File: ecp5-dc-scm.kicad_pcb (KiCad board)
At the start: 8 copper layers, 90 x 120.4 mm, 463 parts, among them IC1 TPS54561, J1 L834-1G1T-S7, J2 1-2199230-6, J3 543630489, J4 M20-7830642, J5 SFF-TA-1002-4C+, J6 0878311420, J7 61300611121, J8 S2B-PH-K-S_LF__SN_, Q1 2N7002, Q10 2N7002, Q11 2N7002, Q12 2N7002, Q13 2N7002, Q14 2N7002, Q15 2N7002, Q16 2N7002, Q17 2N7002, Q2 2N7002, Q3 2N7002, Q4 IRLML6402TRPBF, Q5 IRLML6402TRPBF, Q6 IRLML6402TRPBF, Q7 IRLML6402TRPBF, Q8 IRLML6402TRPBF, Q9 IRLML6402TRPBF, U1 KSZ9031RNXCA, U10 AS4C256M16D3, U11 TPS51200DRC, U12 LM3881MME_NOPB, U13 LM21212-2, U14 SN74LVC1G11DBVR, U16 TPS62823DLCT, U17 TPS62823DLCT, U18 TPS62823DLCT, U19 TPS62823DLCT, U2 W25Q32JVSSIQ_TR, U20 TPS62823DLCT, U21 ECP5UM5G_85_CABGA756, U3 W25Q32JVSSIQ_TR, U4 W25Q32JVSSIQ_TR, U5 W25Q32JVSSIQ_TR, U6 MTFC32GAPALBH-AIT, U7 NVT2008DQ,115, U8 USB3300-EZK-TR, U9 USB3300-EZK-TR, Y1 ABM8G-25.000MHZ-18-D2Y-T, Y2 TSX-3225, Y3 TSX-3225

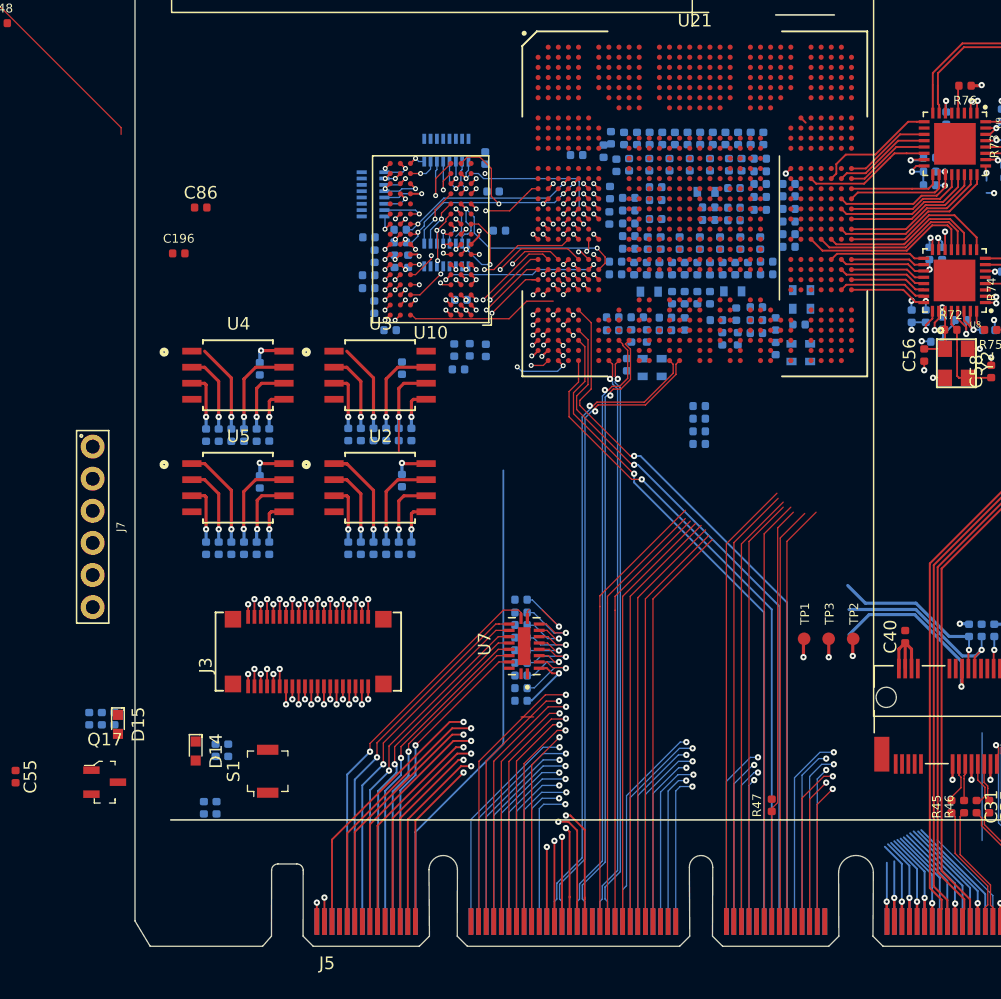
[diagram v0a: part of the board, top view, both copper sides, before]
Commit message: Routed NCSI chip corner
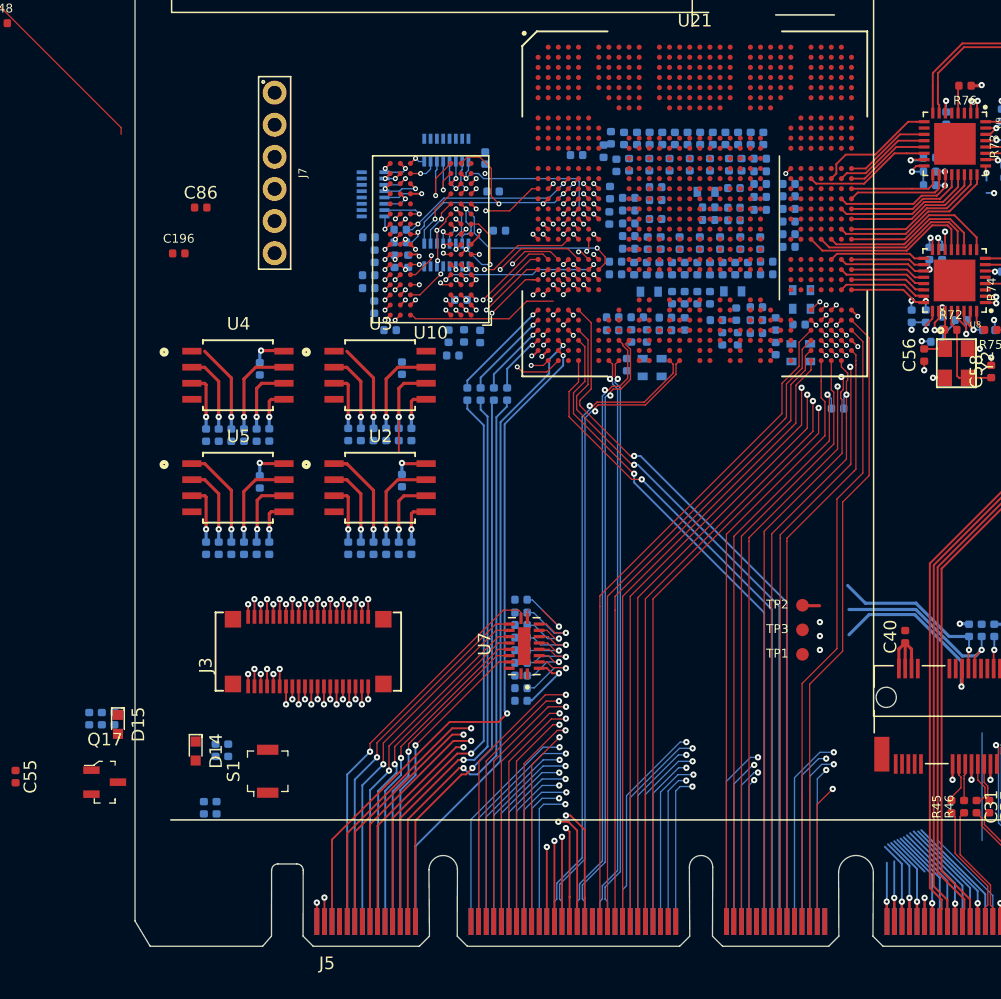
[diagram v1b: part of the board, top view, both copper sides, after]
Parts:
- R47: moved to B.Cu
- moved R47 31.8 mm to (115.7, 136.8), turned to 180 degrees
- moved J7 31.5 mm to (71.2, 118.1)
- moved R132 18.4 mm to (86.4, 135.6), turned to 90 degrees
- moved R133 17.7 mm to (87.5, 135.6), turned to 90 degrees
- moved R135 16.5 mm to (88.5, 135.6), turned to 90 degrees
- moved R134 15.3 mm to (89.5, 135.6), turned to 90 degrees
- moved TP2 4.88 mm to (112.9, 152.3), turned to 180 degrees
- moved TP3 2.26 mm to (112.9, 154.2), turned to 180 degrees
- moved TP1 1.19 mm to (112.9, 156.1), turned to 180 degrees
- moved C80 1.19 mm to (87.4, 131.0)
- moved C84 1.19 mm to (85.2, 132.6)
- moved C85 1.19 mm to (86.1, 131.0)
- moved C87 1.19 mm to (84.9, 131.0)
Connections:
- U21 pad AG28: QSPI1_CS0_N -> QSPI1_D0
- U21 pad AG29: SGPIO0_CLK -> QSPI1_D1
- U21 pad AG30: SGPIO1_CLK -> QSPI1_D2
- U21 pad AG32: SGPIO_RESET_N -> QSPI1_D3
- U21 pad AH28: SGPIO0_DI -> NCSI_TXD1
- U21 pad AH30: SGPIO0_DO -> NCSI_RXER
- U21 pad AH32: SGPIO1_DO -> SGPIO_INTR_N
- U21 pad AJ28: QSPI1_CLK -> NCSI_CLK
- U21 pad AJ29: SGPIO1_LD -> NCSI_RXD0
- U21 pad AJ30: SGPIO_INTR_N -> SGPIO1_DO
- U21 pad AJ31: QSPI1_D1 -> QSPI1_CLK
- U21 pad AJ32: NCSI_TXD0 -> SGPIO_RESET_N
- U21 pad AK29: SGPIO0_LD -> NCSI_RXD1
- U21 pad AK30: SGPIO1_DI -> SGPIO0_CLK
- U21 pad AK31: QSPI1_D3 -> SGPIO1_DI
- U21 pad AK32: NCSI_TXEN -> QSPI1_CS0_N
- U21 pad AL28: NCSI_RXD1 -> NCSI_TXEN
- U21 pad AL30: NCSI_TXD1 -> SGPIO0_LD
- U21 pad AL32: QSPI1_D0 -> SGPIO1_LD
- U21 pad AM28: NCSI_RXD0 -> NCSI_TXD0
- U21 pad AM29: NCSI_CLK -> SGPIO0_DO
- U21 pad AM30: NCSI_RXER -> SGPIO0_DI
- U21 pad AM31: QSPI1_D2 -> SGPIO1_CLK
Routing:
- net (no net): track 49.1 -> 145.2 mm
- net SGPIO_INTR_N: track 42.2 -> 100.6 mm, vias 1 -> 0
- net SGPIO_RESET_N: track 42.2 -> 97.3 mm, vias 1 -> 0
- net I2C[11]_SCL: track 42.7 -> 93.7 mm
- net I2C[12]_SCL: track 42.1 -> 92.5 mm
- net I2C[12]_SDA: track 41.6 -> 92.0 mm
- net I2C[11]_SDA: track 42.7 -> 93.0 mm
- net I2C[9]_SDA: track 46.6 -> 96.1 mm
- net I2C[10]_SDA: track 45.8 -> 95.2 mm
- net I2C[10]_SCL: track 46.3 -> 95.5 mm
- net UART1_SCM_RX: track 64.9 -> 113.0 mm
- net I3C[3]_SDA_3V3: track 41.5 -> 89.5 mm
- net UART0_SCM_TX: track 64.2 -> 112.2 mm
- net ESPI_CS1_N: track 61.3 -> 109.3 mm
- net I3C[2]_SDA_3V3: track 40.2 -> 88.3 mm
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
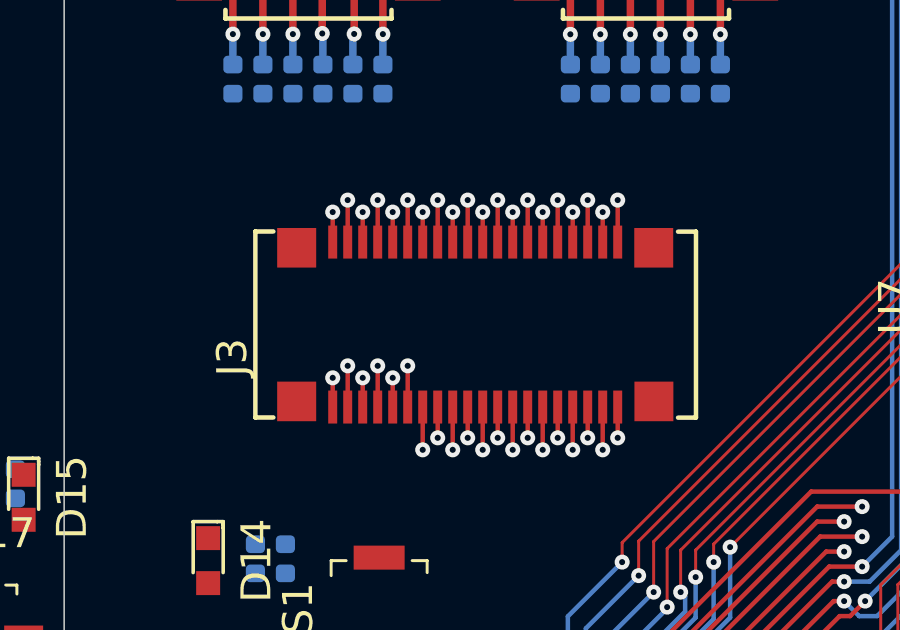
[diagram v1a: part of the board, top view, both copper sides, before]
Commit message: Updated RoT connector
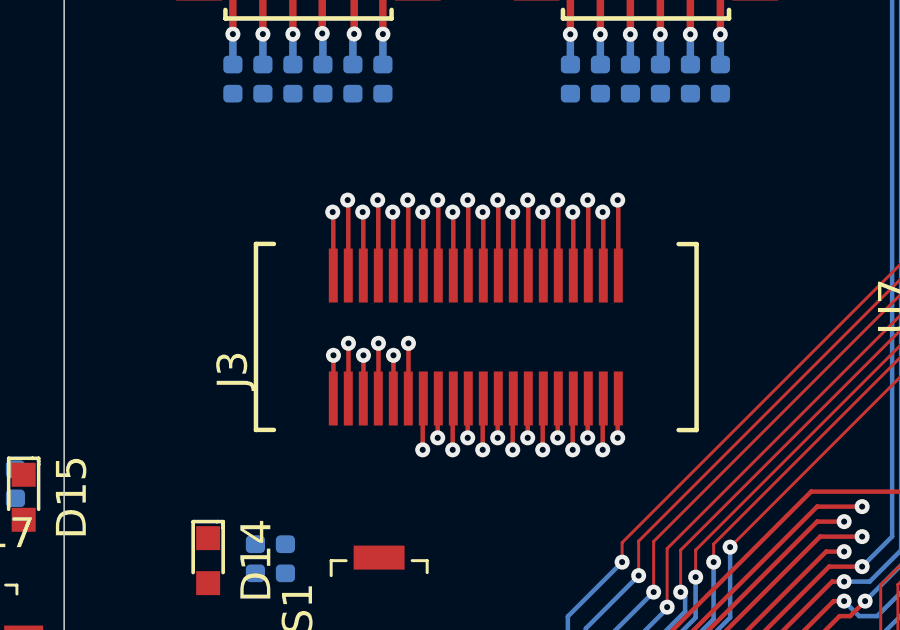
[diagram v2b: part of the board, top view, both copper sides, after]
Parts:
- J3: value 543630489 -> 529910408; footprint ecp5-dc-scm-footprints:543630489 -> ecp5-dc-scm-footprints:529910408
- moved J3 0.42 mm to (73.8, 156.4)
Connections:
- U21 pad A14: RGMII_TXD0 -> Net-(U21-PadA14)
- U21 pad A16: RGMII_RXD0 -> Net-(U21-PadA16)
- U21 pad A17: RGMII_RX_CLK -> Net-(U21-PadA17)
- U21 pad A8: RGMII_TXD1 -> Net-(U21-PadA8)
- U21 pad B16: ETH_MDC -> Net-(U21-PadB16)
- U21 pad B17: RGMII_REF_CLK -> Net-(U21-PadB17)
- U21 pad B8: RGMII_TXD2 -> Net-(U21-PadB8)
- U21 pad C16: RGMII_RX_DV -> Net-(U21-PadC16)
- U21 pad C17: RGMII_TX_CLK -> Net-(U21-PadC17)
- U21 pad C8: RGMII_RXD3 -> Net-(U21-PadC8)
- U21 pad D15: RGMII_TX_EN -> Net-(U21-PadD15)
- U21 pad D16: RGMII_RXD1 -> Net-(U21-PadD16)
- U21 pad D8: RGMII_TXD3 -> Net-(U21-PadD8)
- U21 pad E16: RGMII_RXD2 -> Net-(U21-PadE16)
- U21 pad K12: VCC3V3_T -> Net-(U21-PadK12)
- U21 pad K14: VCC3V3_T -> Net-(U21-PadK14)
- U21 pad K15: VCC3V3_T -> Net-(U21-PadK15)
- U21 pad K16: VCC3V3_T -> Net-(U21-PadK16)
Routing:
- net QSPI0_CS1_N: track 1.40 -> 2.52 mm
- net QSPIA2_D2: track 23.4 -> 24.5 mm
- net VCC3V3: track 64.6 -> 65.7 mm
- net QSPIA2_D1: track 24.7 -> 25.8 mm
- net QSPIB2_D3: track 15.7 -> 16.8 mm
- net QSPIB2_D1: track 14.1 -> 15.2 mm
- net QSPIB2_D0: track 12.0 -> 13.1 mm
- net QSPIB1_D3: track 25.6 -> 26.7 mm
- net QSPIB1_D2: track 22.2 -> 23.3 mm
- net QSPIB1_D0: track 22.2 -> 23.3 mm
- net QSPIB1_CS_N: track 24.9 -> 26.0 mm
- net QSPIA_CLK: track 28.6 -> 29.7 mm
- net QSPIA2_CS_N: track 25.0 -> 26.1 mm
- net ROT_QSPI_CS_N: track 33.2 -> 34.3 mm
- net QSPIB2_CS_N: track 17.0 -> 18.1 mm
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
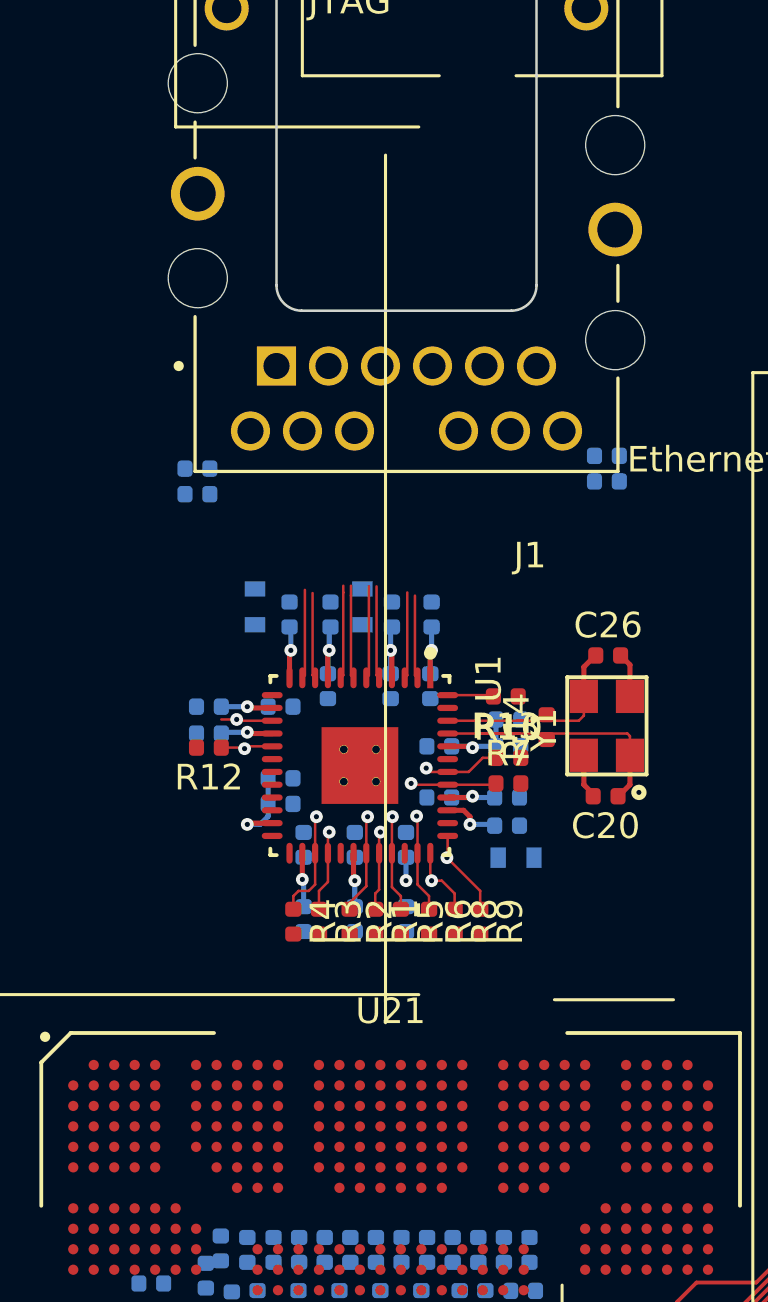
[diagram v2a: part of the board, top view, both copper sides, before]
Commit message: ETH breakout
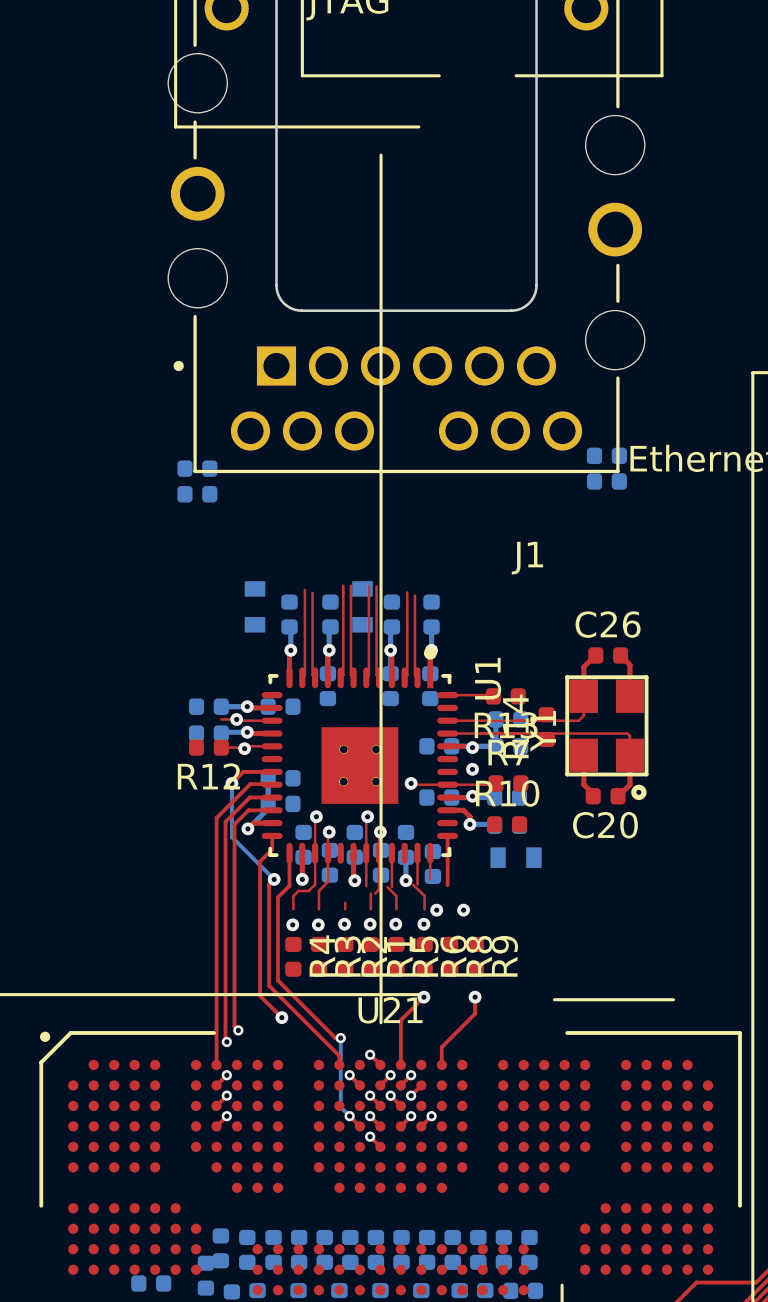
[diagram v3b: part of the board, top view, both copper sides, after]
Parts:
- moved C3 3.74 mm to (104.0, 100.2), turned to 90 degrees
- moved R10 2.60 mm to (109.0, 98.8)
- moved C1 2.41 mm to (102.0, 100.2), turned to 90 degrees
- moved C17 2.39 mm to (106.0, 100.3), turned to 90 degrees
- moved R6 1.39 mm to (105.7, 103.9)
- moved R8 1.39 mm to (106.7, 103.9)
- moved R9 1.39 mm to (107.7, 103.9)
- moved R1 1.39 mm to (103.6, 103.9)
- moved R2 1.39 mm to (102.6, 103.9)
- moved R5 1.39 mm to (104.6, 103.9)
- moved R3 1.38 mm to (101.6, 103.9)
- moved R4 1.38 mm to (100.6, 103.9)
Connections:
- U21 pad A14: Net-(U21-PadA14) -> RGMII_TXD0
- U21 pad A16: Net-(U21-PadA16) -> RGMII_RXD0
- U21 pad A17: Net-(U21-PadA17) -> RGMII_RX_CLK
- U21 pad A8: Net-(U21-PadA8) -> RGMII_TXD1
- U21 pad B16: Net-(U21-PadB16) -> ETH_MDC
- U21 pad B17: Net-(U21-PadB17) -> RGMII_REF_CLK
- U21 pad B8: Net-(U21-PadB8) -> RGMII_TXD2
- U21 pad C16: Net-(U21-PadC16) -> RGMII_RX_DV
- U21 pad C17: Net-(U21-PadC17) -> RGMII_TX_CLK
- U21 pad C8: Net-(U21-PadC8) -> RGMII_RXD3
- U21 pad D15: Net-(U21-PadD15) -> RGMII_TX_EN
- U21 pad D16: Net-(U21-PadD16) -> RGMII_RXD1
- U21 pad D8: Net-(U21-PadD8) -> RGMII_TXD3
- U21 pad E16: Net-(U21-PadE16) -> RGMII_RXD2
- U21 pad K12: Net-(U21-PadK12) -> VCC3V3_T
- U21 pad K14: Net-(U21-PadK14) -> VCC3V3_T
- U21 pad K15: Net-(U21-PadK15) -> VCC3V3_T
- U21 pad K16: Net-(U21-PadK16) -> VCC3V3_T
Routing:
- net ETH_~RESET: track 3.01 -> 18.0 mm, vias 1 -> 2
- net RGMII_TXD0: track 0.00 -> 14.7 mm, vias 0 -> 2
- net RGMII_TXD3: track 0.00 -> 13.9 mm, vias 0 -> 2
- net RGMII_TX_CLK: track 0.00 -> 13.8 mm, vias 0 -> 2
- net RGMII_TXD2: track 0.00 -> 12.7 mm, vias 0 -> 2
- net RGMII_TXD1: track 0.00 -> 12.4 mm
- net RGMII_TX_EN: track 0.00 -> 12.3 mm, vias 0 -> 2
- net RGMII_REF_CLK: track 3.36 -> 15.6 mm, vias 1 -> 2
- net RGMII_RXD2: track 3.18 -> 13.2 mm, vias 1 -> 3
- net RGMII_RXD3: track 4.22 -> 12.5 mm, vias 1 -> 3
- net ETH_MDIO: track 3.41 -> 11.4 mm, vias 1 -> 2
- net RGMII_RXD1: track 3.90 -> 11.5 mm, vias 1 -> 3
- net RGMII_RX_DV: track 3.72 -> 10.0 mm, vias 1 -> 2
- net ETH_MDC: track 2.82 -> 8.78 mm, vias 1 -> 2
- net RGMII_RXD0: track 3.10 -> 8.76 mm, vias 1 -> 3
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
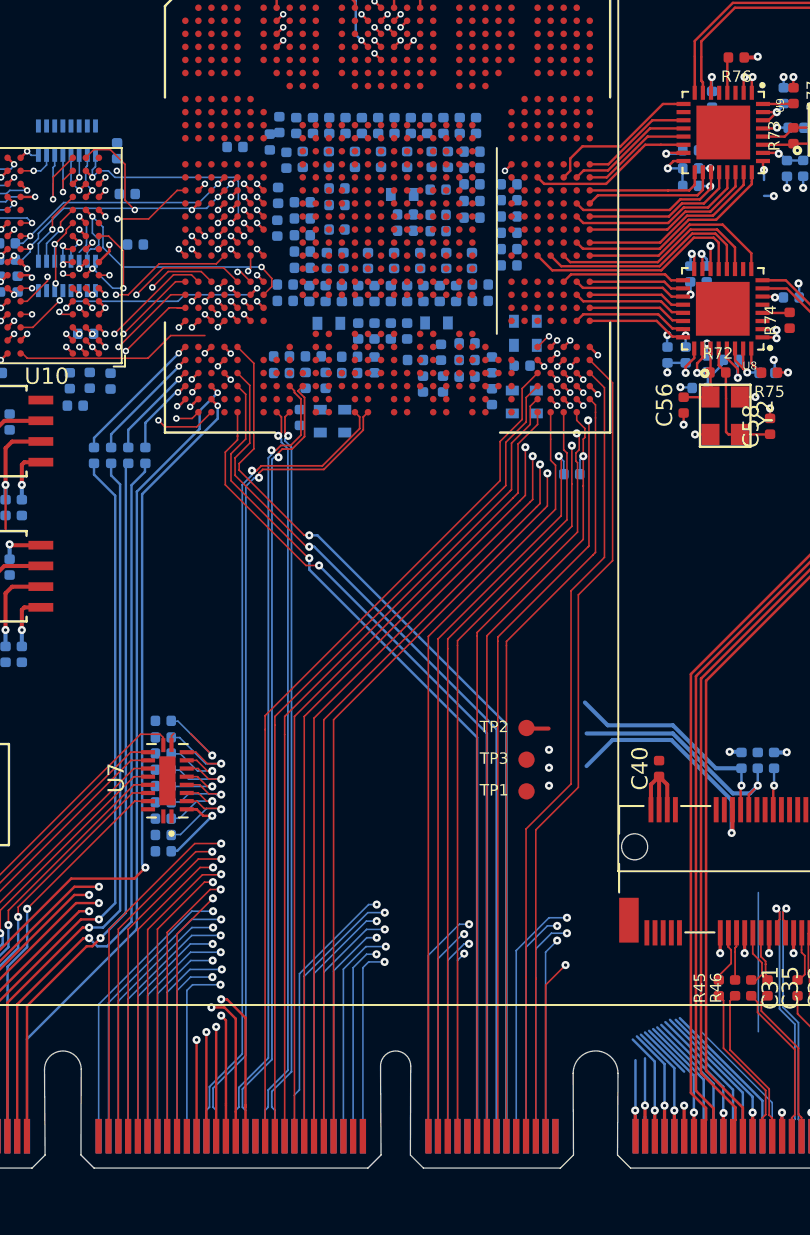
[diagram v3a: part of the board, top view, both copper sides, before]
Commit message: ESPI routed
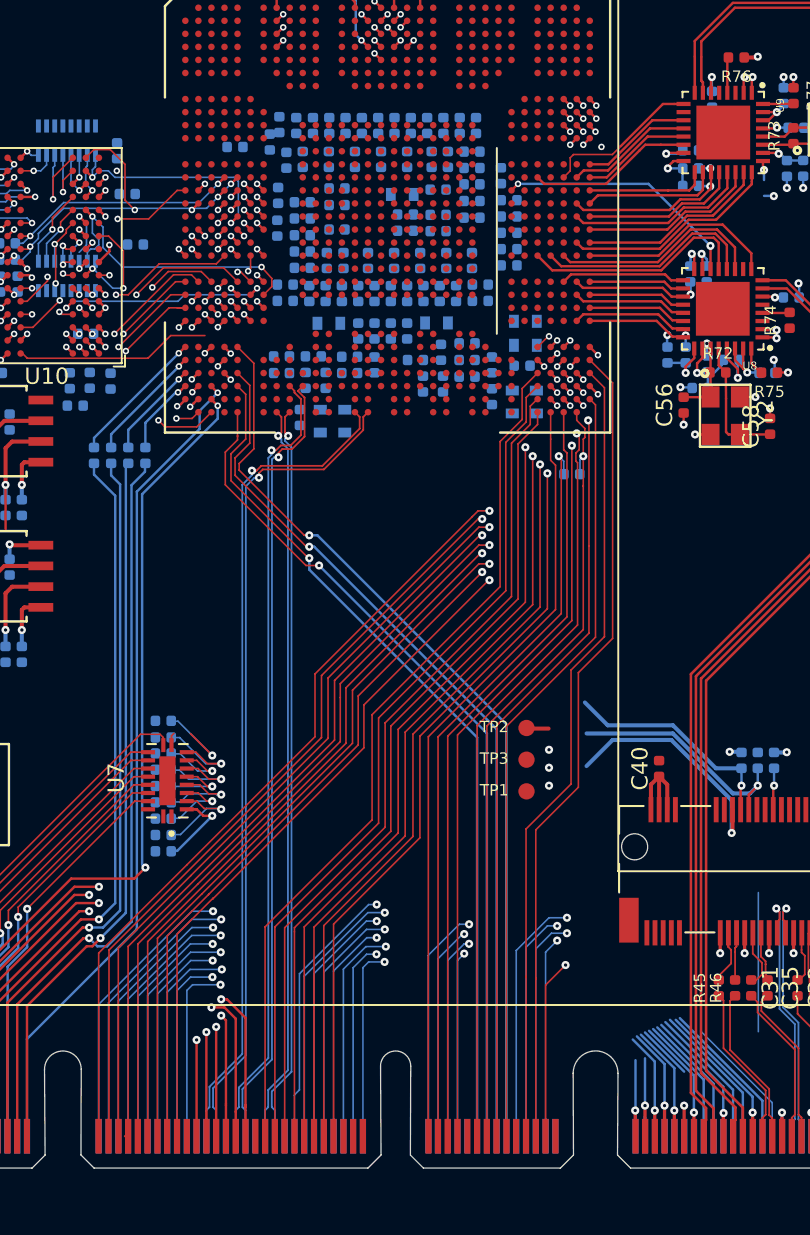
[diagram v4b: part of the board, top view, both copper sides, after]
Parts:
- moved C219 0.72 mm to (111.3, 118.5), turned to 90 degrees
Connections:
- U21 pad D32: ESPI_RESET_N -> Net-(U21-PadD32)
- U21 pad E32: ESPI_IO2 -> Net-(U21-PadE32)
- U21 pad F31: ESPI_ALERT_N -> Net-(U21-PadF31)
- U21 pad F32: ESPI_IO3 -> Net-(U21-PadF32)
- U21 pad H30: ESPI_CS0_N -> ESPI_RESET_N
- U21 pad H31: ESPI_IO0 -> ESPI_IO3
- U21 pad H32: ESPI_IO1 -> ESPI_CS1_N
- U21 pad J30: ESPI_CS1_N -> Net-(U21-PadJ30)
- U21 pad J32: Net-(U21-PadJ32) -> ESPI_IO2
- U21 pad K30: ESPI_CLK -> ESPI_ALERT_N
- U21 pad K31: Net-(U21-PadK31) -> ESPI_IO1
- U21 pad K32: Net-(U21-PadK32) -> ESPI_IO0
- U21 pad L31: Net-(U21-PadL31) -> ESPI_CLK
- U21 pad L32: Net-(U21-PadL32) -> ESPI_CS0_N
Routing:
- net ESPI_CLK: track 0.00 -> 77.6 mm, vias 0 -> 2
- net ESPI_IO2: track 110.5 -> 77.7 mm, vias 1 -> 2
- net ESPI_IO0: track 109.0 -> 77.1 mm, vias 1 -> 2
- net ESPI_IO1: track 110.1 -> 78.3 mm, vias 1 -> 2
- net ESPI_IO3: track 109.8 -> 78.8 mm, vias 1 -> 2
- net ESPI_CS0_N: track 107.1 -> 77.1 mm, vias 1 -> 2
- net ESPI_ALERT_N: track 107.1 -> 78.5 mm, vias 1 -> 2
- net ESPI_RESET_N: track 108.4 -> 80.6 mm, vias 1 -> 3
- net ESPI_CS1_N: track 109.3 -> 126.0 mm, vias 1 -> 2
- net ULPI2_CLKO: track 16.5 -> 15.4 mm
- net VCC3V3: track 64.8 -> 64.2 mm, vias 21 -> 20
- net GND: track 104.0 -> 104.6 mm, vias 87 -> 88
- net Net-(U21-PadJ30): track 0.00 -> 0.57 mm, vias 0 -> 1
